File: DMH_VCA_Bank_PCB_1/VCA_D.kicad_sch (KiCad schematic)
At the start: 21 parts, among them Q1 BC548, Q2 BC548, U1 TL074

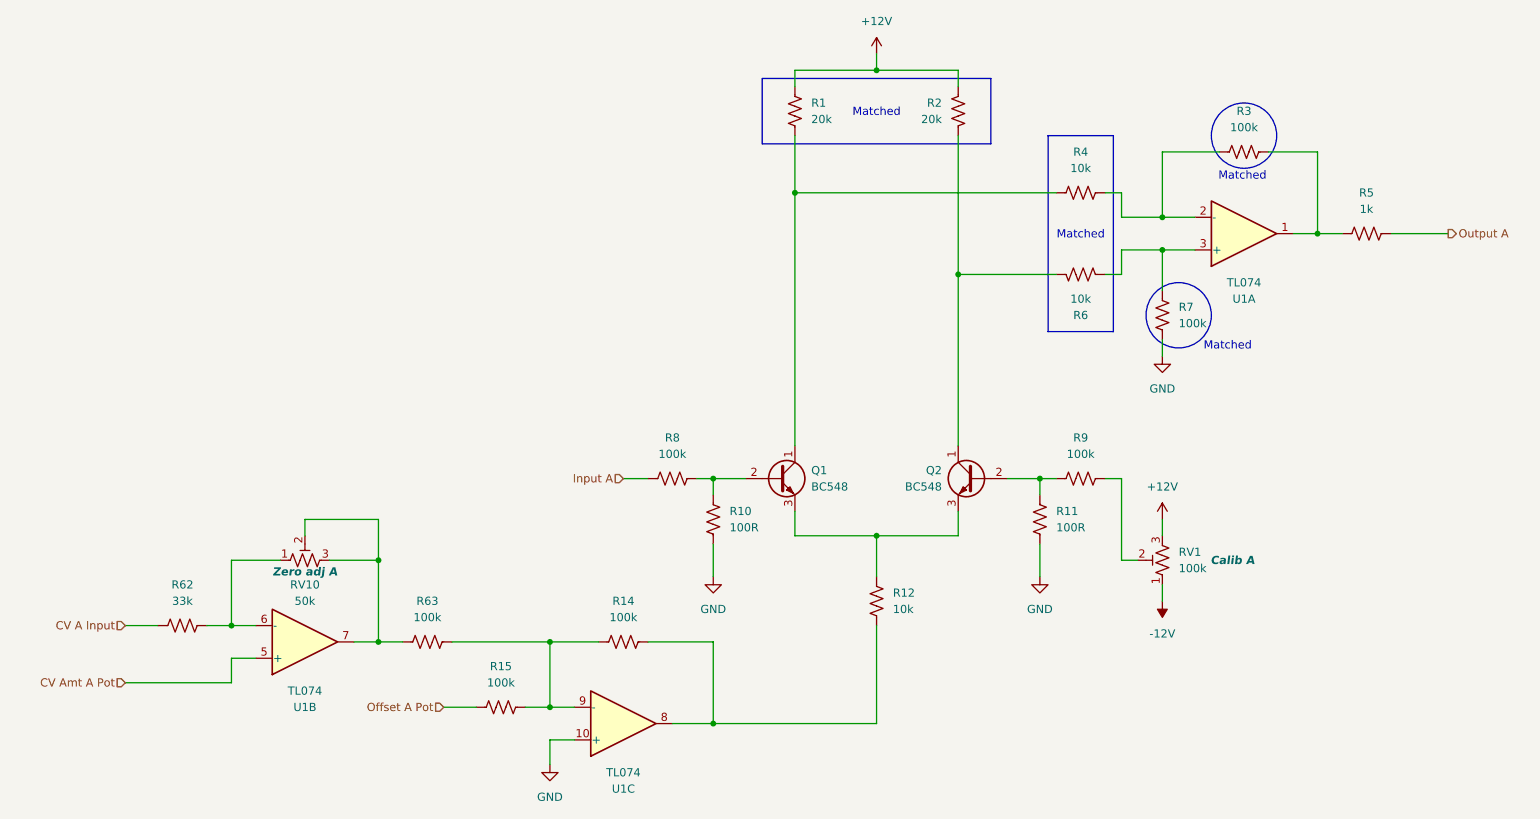
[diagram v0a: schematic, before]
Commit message: Finished schematic of PCB 1
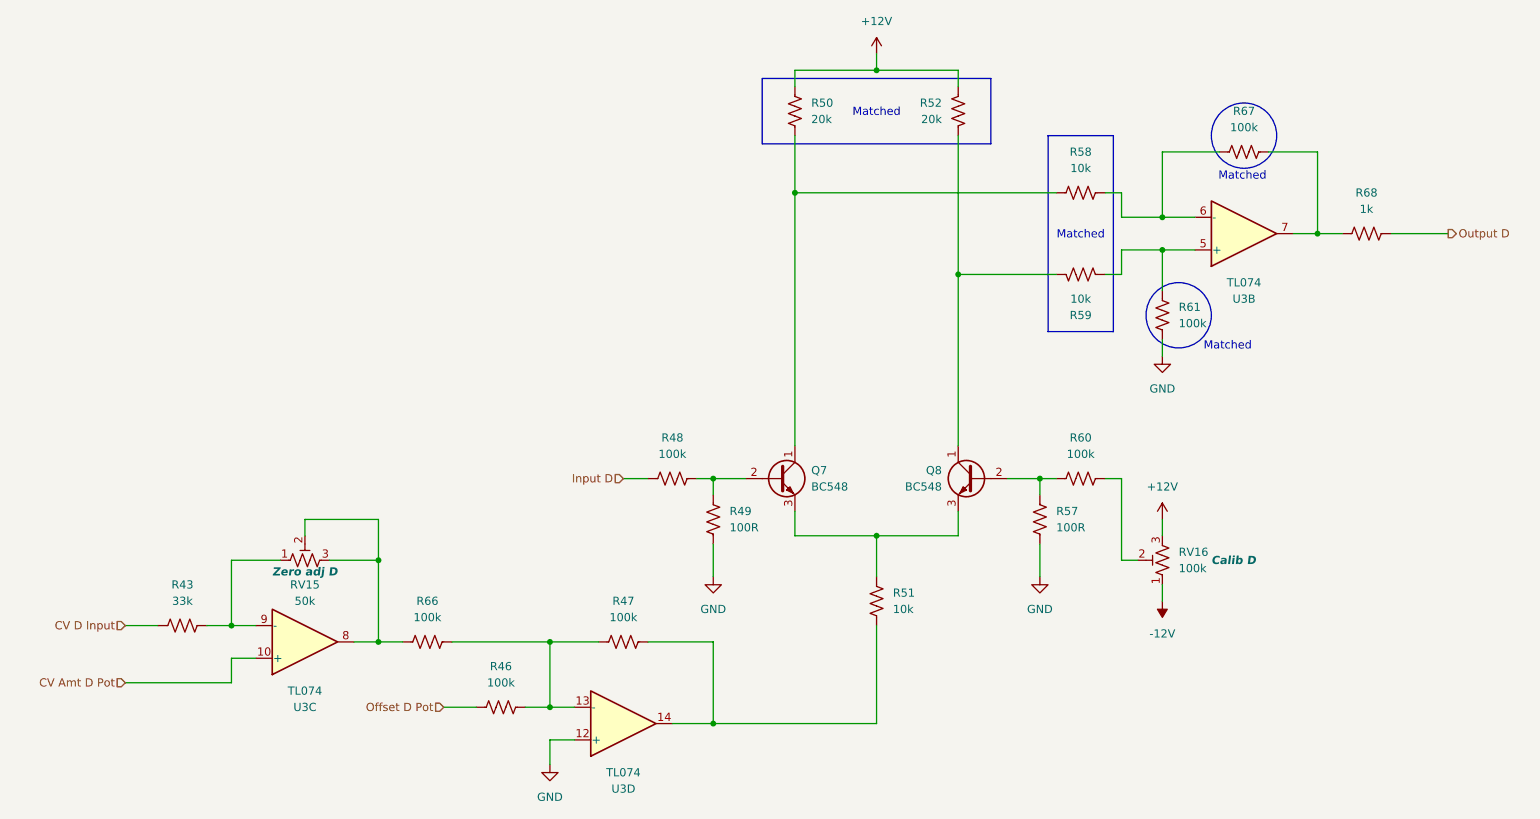
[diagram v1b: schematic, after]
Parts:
- removed R62: 33k, Resistor_THT:R_Axial_DIN0207_L6.3mm_D2.5mm_P2.54mm_Vertical, symbol Device:R_US
- removed R63: 100k, Resistor_THT:R_Axial_DIN0207_L6.3mm_D2.5mm_P2.54mm_Vertical, symbol Device:R_US
- removed RV10: 50k, Potentiometer_THT:Potentiometer_Bourns_3296W_Vertical, symbol Device:R_Potentiometer_Trim_US
- removed unit 2 of U1
- added R43: 33k, Resistor_THT:R_Axial_DIN0207_L6.3mm_D2.5mm_P2.54mm_Vertical, symbol Device:R_US
- added R66: 100k, Resistor_THT:R_Axial_DIN0207_L6.3mm_D2.5mm_P2.54mm_Vertical, symbol Device:R_US
- added RV15: 50k, Potentiometer_THT:Potentiometer_Bourns_3296W_Vertical, symbol Device:R_Potentiometer_Trim_US
- added unit 3 of U3
- RV16: renamed from RV1; Function Calib A -> Calib D
- renumbered Q1 to Q7, Q2 to Q8, R15 to R46, R14 to R47, R8 to R48, R10 to R49, R1 to R50, R12 to R51, R2 to R52, R11 to R57, R4 to R58, R6 to R59, R9 to R60, R7 to R61, R3 to R67, R5 to R68, U1 to U3
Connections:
- net GND: now also U3.12 (+); no longer U3.10 (+)
- net at R67.1, R68.2: now also U3.7; no longer U3.1
- net at R58.1, R67.2: now also U3.6 (-); no longer U3.2 (-)
- net at R59.1, R61.1: now also U3.5 (+); no longer U3.3 (+)
- net at R46.2, R47.1: now also U3.13 (-), R66.2; no longer U3.9 (-)
- net at R47.2, R51.1: now also U3.14; no longer U3.8
- net Input A renamed Input D
- net Offset A Pot renamed Offset D Pot
- net Output A renamed Output D
- new net: R66.1, RV15.2, RV15.3, U3.8
- new net: R43.2, RV15.1, U3.9 (-)
- new net CV Amt D Pot: U3.10 (+)
- new net CV D Input: R43.1
